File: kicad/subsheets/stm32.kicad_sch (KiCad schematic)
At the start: 11 parts, among them U3 STM32U575RGT6

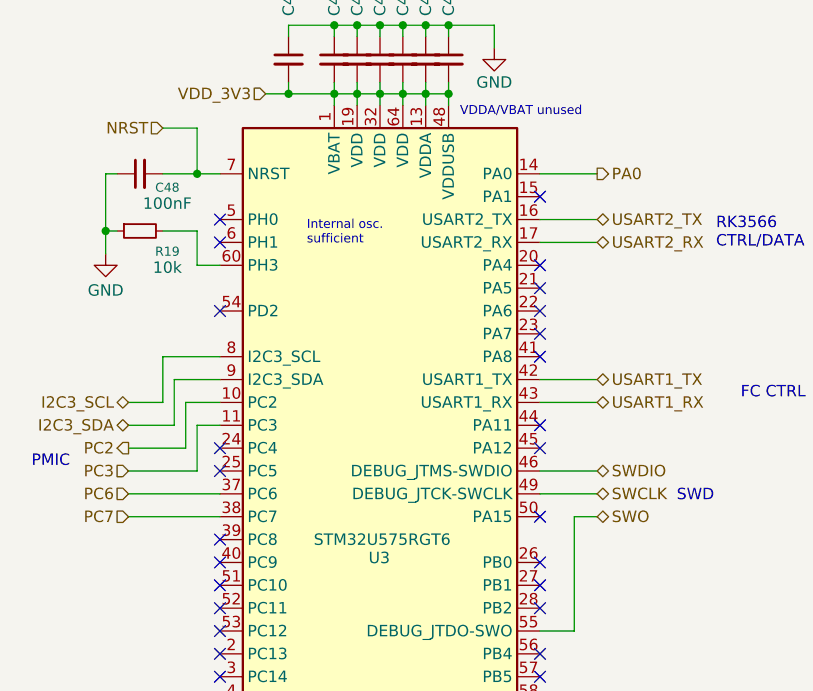
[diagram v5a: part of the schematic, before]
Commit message: Clean up debug connector, STM pinout
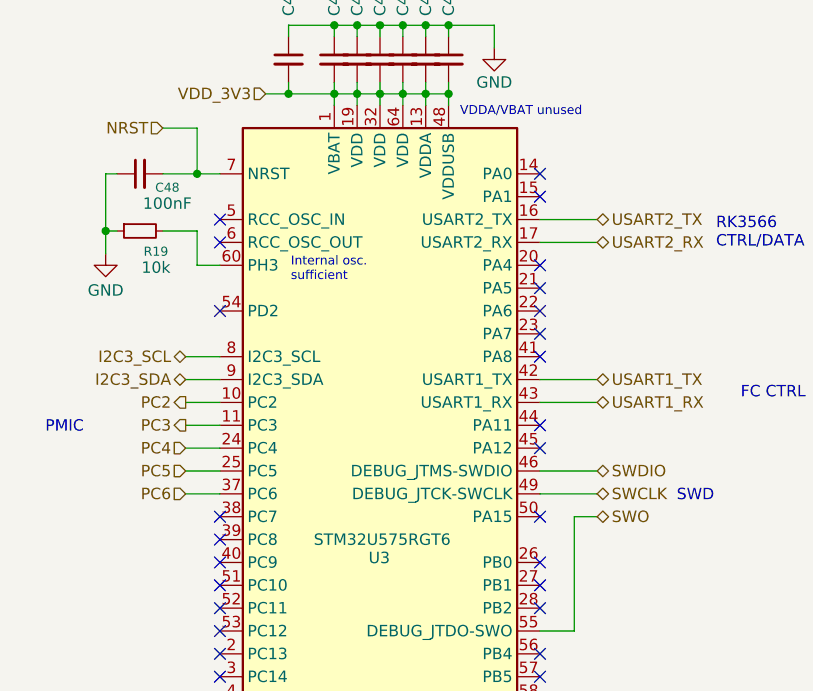
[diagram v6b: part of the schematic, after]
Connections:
- net PC4: now reaches U3.24 (PC4)
- net PC5: now reaches U3.25 (PC5)
- net PA0: no longer names the net of U3.14 (PA0)
- net PC7: no longer names the net of U3.38 (PC7)
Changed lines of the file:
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@@
 	(text "PMIC\n"
 		(exclude_from_sim no)
-		(at 33.274 77.724 0)
+		(at 34.798 73.914 0)
 		(effects
 			(font
@@
 	(text "Internal osc.\nsufficient"
 		(exclude_from_sim no)
-		(at 61.722 52.324 0)
+		(at 59.944 56.388 0)
 		(effects
 			(font
@@
 	)
 	(no_connect
+		(at 87.63 45.72)
+	)
+	(no_connect
 		(at 52.07 88.9)
 	)
@@
 	)
 	(no_connect
+		(at 52.07 86.36)
+	)
+	(no_connect
 		(at 52.07 96.52)
 	)
@@
 	)
 	(no_connect
-		(at 52.07 86.36)
+		(at 52.07 83.82)
 	)
 	(no_connect
@@
 	)
 	(no_connect
-		(at 52.07 76.2)
-	)
-	(no_connect
-		(at 52.07 78.74)
-	)
-	(no_connect
 		(at 87.63 116.84)
 	)
@@
 	(wire
 		(pts
-			(xy 93.98 45.72) (xy 87.63 45.72)
-		)
-		(stroke
-			(width 0)
-			(type default)
-		)
-	)
-	(wire
-		(pts
 			(xy 82.55 29.21) (xy 82.55 31.75)
 		)
@@
 	(wire
 		(pts
-			(xy 41.91 76.2) (xy 48.26 76.2)
+			(xy 48.26 71.12) (xy 52.07 71.12)
 		)
 		(stroke
@@
 	(wire
 		(pts
-			(xy 49.53 78.74) (xy 49.53 73.66)
-		)
-		(stroke
-			(width 0)
-			(type default)
-		)
-	)
-	(wire
-		(pts
 			(xy 39.37 54.61) (xy 39.37 52.07)
 		)
@@
 	(wire
 		(pts
-			(xy 41.91 78.74) (xy 49.53 78.74)
-		)
-		(stroke
-			(width 0)
-			(type default)
-		)
-	)
-	(wire
-		(pts
-			(xy 46.99 73.66) (xy 46.99 68.58)
+			(xy 48.26 73.66) (xy 52.07 73.66)
 		)
 		(stroke
@@
 	(wire
 		(pts
+			(xy 48.26 76.2) (xy 52.07 76.2)
+		)
+		(stroke
+			(width 0)
+			(type default)
+		)
+	)
+	(wire
+		(pts
 			(xy 67.31 36.83) (xy 69.85 36.83)
 		)
@@
 	(wire
 		(pts
-			(xy 48.26 71.12) (xy 52.07 71.12)
-		)
-		(stroke
-			(width 0)
-			(type default)
-		)
-	)
-	(wire
-		(pts
 			(xy 59.69 29.21) (xy 64.77 29.21)
 		)
@@
 	(wire
 		(pts
-			(xy 41.91 71.12) (xy 45.72 71.12)
+			(xy 48.26 66.04) (xy 52.07 66.04)
 		)
 		(stroke
@@
 	(wire
 		(pts
-			(xy 49.53 73.66) (xy 52.07 73.66)
-		)
-		(stroke
-			(width 0)
-			(type default)
-		)
-	)
-	(wire
-		(pts
 			(xy 93.98 104.14) (xy 87.63 104.14)
 		)
@@
 	(wire
 		(pts
+			(xy 48.26 78.74) (xy 52.07 78.74)
+		)
+		(stroke
+			(width 0)
+			(type default)
+		)
+	)
+	(wire
+		(pts
 			(xy 72.39 29.21) (xy 72.39 30.48)
 		)
@@
 	(wire
 		(pts
-			(xy 45.72 71.12) (xy 45.72 66.04)
-		)
-		(stroke
-			(width 0)
-			(type default)
-		)
-	)
-	(wire
-		(pts
 			(xy 68.58 133.35) (xy 68.58 134.62)
 		)
@@
 	(wire
 		(pts
-			(xy 45.72 66.04) (xy 52.07 66.04)
-		)
-		(stroke
-			(width 0)
-			(type default)
-		)
-	)
-	(wire
-		(pts
 			(xy 77.47 35.56) (xy 77.47 36.83)
 		)
@@
 	(wire
 		(pts
-			(xy 48.26 76.2) (xy 48.26 71.12)
-		)
-		(stroke
-			(width 0)
-			(type default)
-		)
-	)
-	(wire
-		(pts
 			(xy 74.93 36.83) (xy 77.47 36.83)
 		)
@@
 	(wire
 		(pts
-			(xy 41.91 83.82) (xy 52.07 83.82)
-		)
-		(stroke
-			(width 0)
-			(type default)
-		)
-	)
-	(wire
-		(pts
 			(xy 57.15 36.83) (xy 59.69 36.83)
 		)
@@
 	(wire
 		(pts
-			(xy 41.91 81.28) (xy 52.07 81.28)
+			(xy 48.26 81.28) (xy 52.07 81.28)
 		)
 		(stroke
@@
 	(wire
 		(pts
-			(xy 41.91 73.66) (xy 46.99 73.66)
+			(xy 48.26 68.58) (xy 52.07 68.58)
 		)
 		(stroke
@@
 		(pts
 			(xy 77.47 36.83) (xy 77.47 38.1)
-		)
-		(stroke
-			(width 0)
-			(type default)
-		)
-	)
-	(wire
-		(pts
-			(xy 46.99 68.58) (xy 52.07 68.58)
 		)
 		(stroke
@@
 	(hierarchical_label "I2C3_SDA"
 		(shape bidirectional)
-		(at 41.91 73.66 180)
+		(at 48.26 68.58 180)
 		(effects
 			(font
@@
 	(hierarchical_label "PC6"
 		(shape input)
-		(at 41.91 81.28 180)
+		(at 48.26 81.28 180)
 		(effects
 			(font
@@
 		)
 	)
+	(hierarchical_label "PC4"
+		(shape input)
+		(at 48.26 76.2 180)
+		(effects
+			(font
+				(size 1.27 1.27)
+			)
+			(justify right)
+		)
+	)
 	(hierarchical_label "I2C3_SCL"
 		(shape bidirectional)
-		(at 41.91 71.12 180)
-		(effects
-			(font
-				(size 1.27 1.27)
-			)
-			(justify right)
-		)
-	)
-	(hierarchical_label "PC7"
-		(shape input)
-		(at 41.91 83.82 180)
+		(at 48.26 66.04 180)
 		(effects
 			(font
@@
 	(hierarchical_label "PC2"
 		(shape output)
-		(at 41.91 76.2 180)
+		(at 48.26 71.12 180)
 		(effects
 			(font
@@
 		)
 	)
+	(hierarchical_label "PC5"
+		(shape input)
+		(at 48.26 78.74 180)
+		(effects
+			(font
+				(size 1.27 1.27)
+			)
+			(justify right)
+		)
+	)
 	(hierarchical_label "PC3"
-		(shape input)
-		(at 41.91 78.74 180)
+		(shape output)
+		(at 48.26 73.66 180)
 		(effects
 			(font
@@
 		(shape bidirectional)
 		(at 93.98 106.68 0)
-		(effects
-			(font
-				(size 1.27 1.27)
-			)
-			(justify left)
-		)
-	)
-	(hierarchical_label "PA0"
-		(shape output)
-		(at 93.98 45.72 0)
 		(effects
 			(font
@@
 		)
 		(pin "5"
+			(alternate "RCC_OSC_IN")
 		)
 		(pin "6"
+			(alternate "RCC_OSC_OUT")
 		)
 		(pin "60"
@@
 		(dnp no)
 		(property "Reference" "R19"
-			(at 46.228 54.356 90)
+			(at 44.958 54.356 90)
 			(effects
 				(font
@@
 		)
 		(property "Value" "10k"
-			(at 46.228 56.134 90)
-			(effects
-				(font
+			(at 44.958 56.134 90)
+			(effects
+				(font

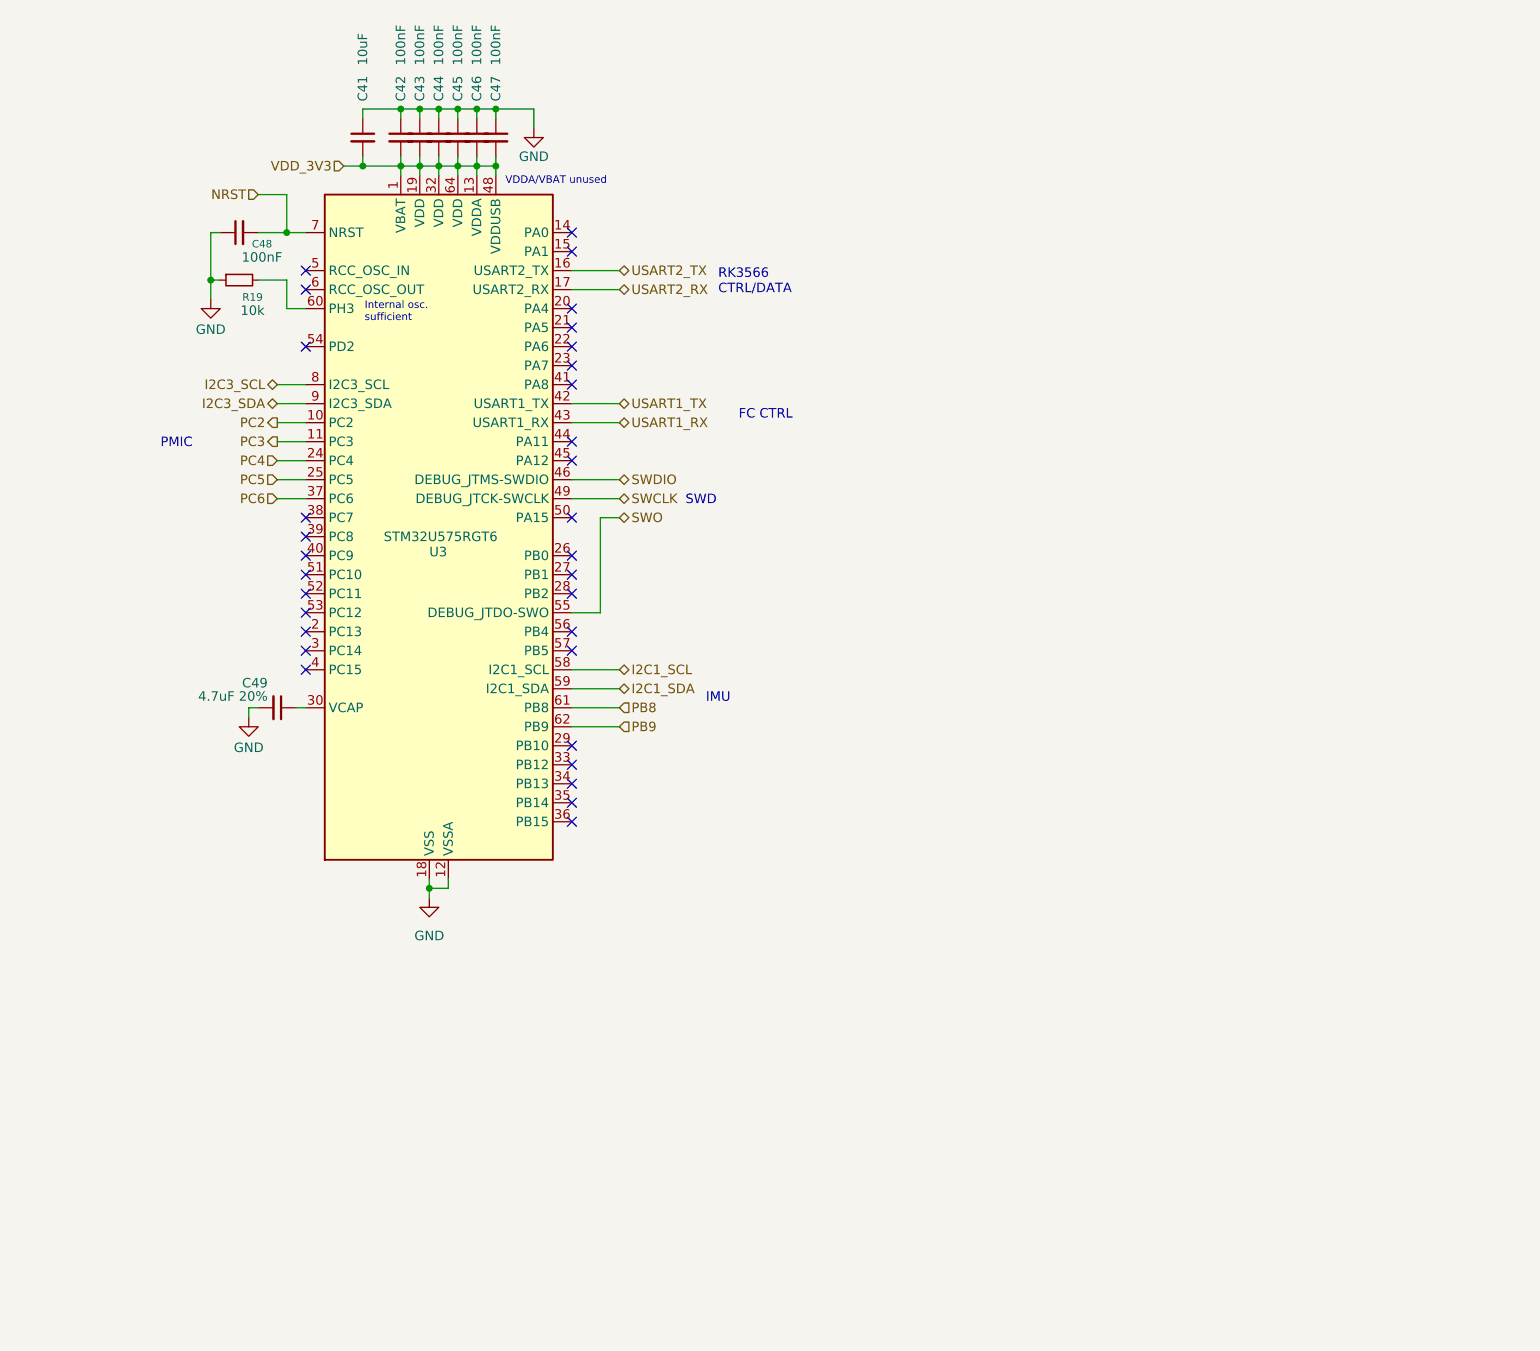
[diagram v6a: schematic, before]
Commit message: Reconfigure STM32 pinout to work better with physical pin locations
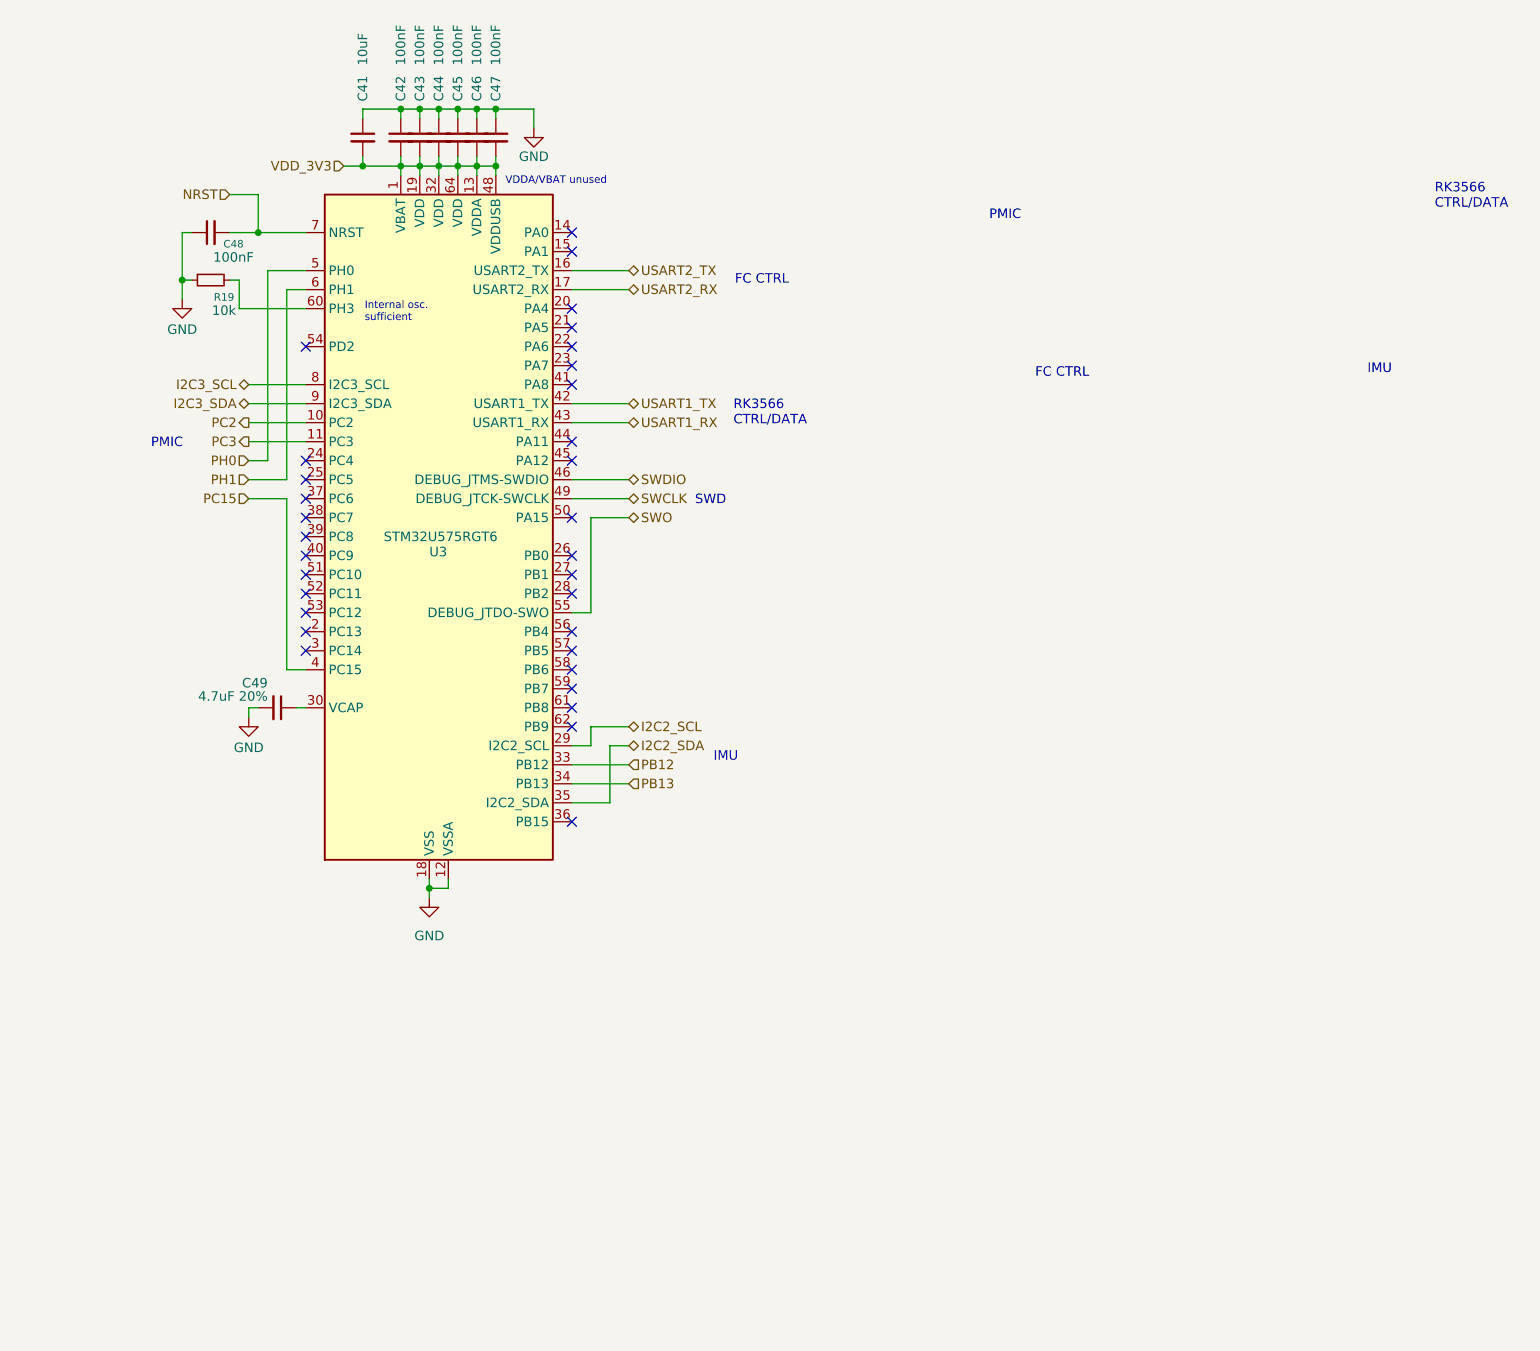
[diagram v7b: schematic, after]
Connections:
- net I2C2_SCL: now reaches U3.29 (PB10)
- net PB12: now reaches U3.33 (PB12)
- net PB13: now reaches U3.34 (PB13)
- net I2C2_SDA: now reaches U3.35 (PB14)
- net PC15: now reaches U3.4 (PC15)
- net PH0: now reaches U3.5 (PH0)
- net PH1: now reaches U3.6 (PH1)
- net I2C1_SCL: no longer names the net of U3.58 (PB6)
- net I2C1_SDA: no longer names the net of U3.59 (PB7)
- net PB8: no longer names the net of U3.61 (PB8)
- net PB9: no longer names the net of U3.62 (PB9)
- net PC4: no longer names the net of U3.24 (PC4)
- net PC5: no longer names the net of U3.25 (PC5)
- net PC6: no longer names the net of U3.37 (PC6)
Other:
- moved on the sheet: C48, R19
